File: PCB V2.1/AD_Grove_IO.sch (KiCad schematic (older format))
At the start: 0 parts

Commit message: SunLeaf Alpha 0.2 and KiCAD Port
SunLeaf rev 2 called Alhpa 0.2 or 0.2a is the main component of this
commit. The entire hardware project has been ported to KiCAD libaries
and all. 0.2a features a revised formfactor, better ESP module, and many
fixes over the original. This version will also be capable of OTA
updates.
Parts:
- added C32, C33, C34, C35: CL05B104JP5NNNC, PCB_Footprints:C0402, symbol CL05B104JP5NNNC
- added D10, D11, D12, D13: PESD3V3L2BT,215, PCB_Footprints:BAT20JFILM, symbol PESD3V3L2BT,215
- added J13, J14, J15, J16: S4B-PH-SM4-TB(LF)(SN), PCB_Footprints:S4B-PH-SM4-TB(LF)(SN), symbol S4B-PH-SM4-TB(LF)(SN)
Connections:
- net labels added: +3.3V, GND
- wire segments 0 -> 30

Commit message: Placement
Heavy progress on component placement in KiCAD for SunLEaf V2,
committing to save progress, nightly builds of KiCAD are very crash
prone.
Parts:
- D10, D11, D12, D13: footprint PCB_Footprints:BAT20JFILM -> PCB_Footprints:PESD3V3L2BT,215
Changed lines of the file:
@@
 F 0 "D10" V 4150 4675 60  0000 C CNN
 F 1 "PESD3V3L2BT,215" H 4375 4350 60  0000 C CNN
-F 2 "PCB_Footprints:BAT20JFILM" H 5650 6450 60  0001 C CNN
+F 2 "PCB_Footprints:PESD3V3L2BT,215" H 5650 6450 60  0001 C CNN
 F 3 "http://www.nxp.com/documents/data_sheet/PESDXL2BT_SER.pdf" H 5850 6575 60  0001 C CNN
 F 4 "0.15109 @ 6000" H 4075 4725 60  0001 C CNN "Cost"
@@
 F 0 "D11" V 4750 4675 60  0000 C CNN
 F 1 "PESD3V3L2BT,215" H 4975 4350 60  0000 C CNN
-F 2 "PCB_Footprints:BAT20JFILM" H 6250 6450 60  0001 C CNN
+F 2 "PCB_Footprints:PESD3V3L2BT,215" H 6250 6450 60  0001 C CNN
 F 3 "http://www.nxp.com/documents/data_sheet/PESDXL2BT_SER.pdf" H 6450 6575 60  0001 C CNN
 F 4 "0.15109 @ 6000" H 4675 4725 60  0001 C CNN "Cost"
@@
 F 0 "D12" V 5350 4675 60  0000 C CNN
 F 1 "PESD3V3L2BT,215" H 5575 4350 60  0000 C CNN
-F 2 "PCB_Footprints:BAT20JFILM" H 6850 6450 60  0001 C CNN
+F 2 "PCB_Footprints:PESD3V3L2BT,215" H 6850 6450 60  0001 C CNN
 F 3 "http://www.nxp.com/documents/data_sheet/PESDXL2BT_SER.pdf" H 7050 6575 60  0001 C CNN
 F 4 "0.15109 @ 6000" H 5275 4725 60  0001 C CNN "Cost"
@@
 F 0 "D13" V 5950 4675 60  0000 C CNN
 F 1 "PESD3V3L2BT,215" H 6175 4350 60  0000 C CNN
-F 2 "PCB_Footprints:BAT20JFILM" H 7450 6450 60  0001 C CNN
+F 2 "PCB_Footprints:PESD3V3L2BT,215" H 7450 6450 60  0001 C CNN
 F 3 "http://www.nxp.com/documents/data_sheet/PESDXL2BT_SER.pdf" H 7650 6575 60  0001 C CNN
 F 4 "0.15109 @ 6000" H 5875 4725 60  0001 C CNN "Cost"
@@
 Connection ~ 6100 2000
 $Comp
-L GND #PWR70
+L GND #PWR73
 U 1 1 57DACA24
 P 4225 4800
-F 0 "#PWR70" H 4225 4550 50  0001 C CNN
+F 0 "#PWR73" H 4225 4550 50  0001 C CNN
 F 1 "GND" H 4225 4650 50  0000 C CNN
 F 2 "" H 4225 4800 50  0000 C CNN
@@
 $EndComp
 $Comp
-L GND #PWR71
+L GND #PWR74
 U 1 1 57DACA56
 P 4825 4800
-F 0 "#PWR71" H 4825 4550 50  0001 C CNN
+F 0 "#PWR74" H 4825 4550 50  0001 C CNN
 F 1 "GND" H 4825 4650 50  0000 C CNN
 F 2 "" H 4825 4800 50  0000 C CNN
@@
 $EndComp
 $Comp
-L GND #PWR72
+L GND #PWR75
 U 1 1 57DACA7C
 P 5425 4800
-F 0 "#PWR72" H 5425 4550 50  0001 C CNN
+F 0 "#PWR75" H 5425 4550 50  0001 C CNN
 F 1 "GND" H 5425 4650 50  0000 C CNN
 F 2 "" H 5425 4800 50  0000 C CNN
@@
 $EndComp
 $Comp
-L GND #PWR73
+L GND #PWR76
 U 1 1 57DACAA2
 P 6025 4800
-F 0 "#PWR73" H 6025 4550 50  0001 C CNN
+F 0 "#PWR76" H 6025 4550 50  0001 C CNN
 F 1 "GND" H 6025 4650 50  0000 C CNN
 F 2 "" H 6025 4800 50  0000 C CNN
@@
 $EndComp
 $Comp
-L GND #PWR83
+L GND #PWR86
 U 1 1 57DACCA5
 P 10050 3675
-F 0 "#PWR83" H 10050 3425 50  0001 C CNN
+F 0 "#PWR86" H 10050 3425 50  0001 C CNN
 F 1 "GND" H 10050 3525 50  0000 C CNN
 F 2 "" H 10050 3675 50  0000 C CNN
@@
 $EndComp
 $Comp
-L GND #PWR82
+L GND #PWR85
 U 1 1 57DAD2A3
 P 10050 2975
-F 0 "#PWR82" H 10050 2725 50  0001 C CNN
+F 0 "#PWR85" H 10050 2725 50  0001 C CNN
 F 1 "GND" H 10050 2825 50  0000 C CNN
 F 2 "" H 10050 2975 50  0000 C CNN
@@
 $EndComp
 $Comp
-L GND #PWR81
+L GND #PWR84
 U 1 1 57DAD311
 P 10050 2250
-F 0 "#PWR81" H 10050 2000 50  0001 C CNN
+F 0 "#PWR84" H 10050 2000 50  0001 C CNN
 F 1 "GND" H 10050 2100 50  0000 C CNN
 F 2 "" H 10050 2250 50  0000 C CNN
@@
 $EndComp
 $Comp
-L GND #PWR80
+L GND #PWR83
 U 1 1 57DAD3C7
 P 10050 1525
-F 0 "#PWR80" H 10050 1275 50  0001 C CNN
+F 0 "#PWR83" H 10050 1275 50  0001 C CNN
 F 1 "GND" H 10050 1375 50  0000 C CNN
 F 2 "" H 10050 1525 50  0000 C CNN
@@
 	9950 1525 9950 1775
 $Comp
-L +3.3V #PWR76
+L +3.3V #PWR79
 U 1 1 57DAD7A9
 P 9700 4000
-F 0 "#PWR76" H 9700 3850 50  0001 C CNN
+F 0 "#PWR79" H 9700 3850 50  0001 C CNN
 F 1 "+3.3V" H 9700 4140 50  0000 C CNN
 F 2 "" H 9700 4000 50  0000 C CNN
@@
 	9700 4000 9950 4000
 $Comp
-L +3.3V #PWR79
+L +3.3V #PWR82
 U 1 1 57DAD8CB
 P 9725 3300
-F 0 "#PWR79" H 9725 3150 50  0001 C CNN
+F 0 "#PWR82" H 9725 3150 50  0001 C CNN
 F 1 "+3.3V" H 9725 3440 50  0000 C CNN
 F 2 "" H 9725 3300 50  0000 C CNN
@@
 	9950 3300 9725 3300
 $Comp
-L +3.3V #PWR78
+L +3.3V #PWR81
 U 1 1 57DAD9D1
 P 9725 2575
-F 0 "#PWR78" H 9725 2425 50  0001 C CNN
+F 0 "#PWR81" H 9725 2425 50  0001 C CNN
 F 1 "+3.3V" H 9725 2715 50  0000 C CNN
 F 2 "" H 9725 2575 50  0000 C CNN
@@
 	9725 2575 9950 2575
 $Comp
-L +3.3V #PWR77
+L +3.3V #PWR80
 U 1 1 57DADAE1
 P 9725 1850
-F 0 "#PWR77" H 9725 1700 50  0001 C CNN
+F 0 "#PWR80" H 9725 1700 50  0001 C CNN
 F 1 "+3.3V" H 9725 1990 50  0000 C CNN
 F 2 "" H 9725 1850 50  0000 C CNN
@@
 Connection ~ 9575 4475
 $Comp
-L +3.3V #PWR74
+L +3.3V #PWR77
 U 1 1 57DAE2C9
 P 9400 4475
-F 0 "#PWR74" H 9400 4325 50  0001 C CNN
+F 0 "#PWR77" H 9400 4325 50  0001 C CNN
 F 1 "+3.3V" H 9400 4615 50  0000 C CNN
 F 2 "" H 9400 4475 50  0000 C CNN
@@
 $EndComp
 $Comp
-L GND #PWR75
+L GND #PWR78
 U 1 1 57DAE2F8
 P 9400 4925
-F 0 "#PWR75" H 9400 4675 50  0001 C CNN
+F 0 "#PWR78" H 9400 4675 50  0001 C CNN
 F 1 "GND" H 9400 4775 50  0000 C CNN
 F 2 "" H 9400 4925 50  0000 C CNN

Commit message: Placement progress
Placement is 99% done board is being resized. Next commit TVS diode
pairs will be fliped and the baord further resized.
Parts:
- removed C32, C33, C34, C35: CL05B104JP5NNNC, PCB_Footprints:C0402, symbol CL05B104JP5NNNC
- removed J13, J14, J15, J16: S4B-PH-SM4-TB(LF)(SN), PCB_Footprints:S4B-PH-SM4-TB(LF)(SN), symbol S4B-PH-SM4-TB(LF)(SN)
- added J13, J14, J15, J16: B4B-PH-K-S(LF)(SN), PCB_Footprints:B4B-PH-K-S(LF)(SN), symbol B4B-PH-K-S(LF)(SN)
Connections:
- wire segments 30 -> 28

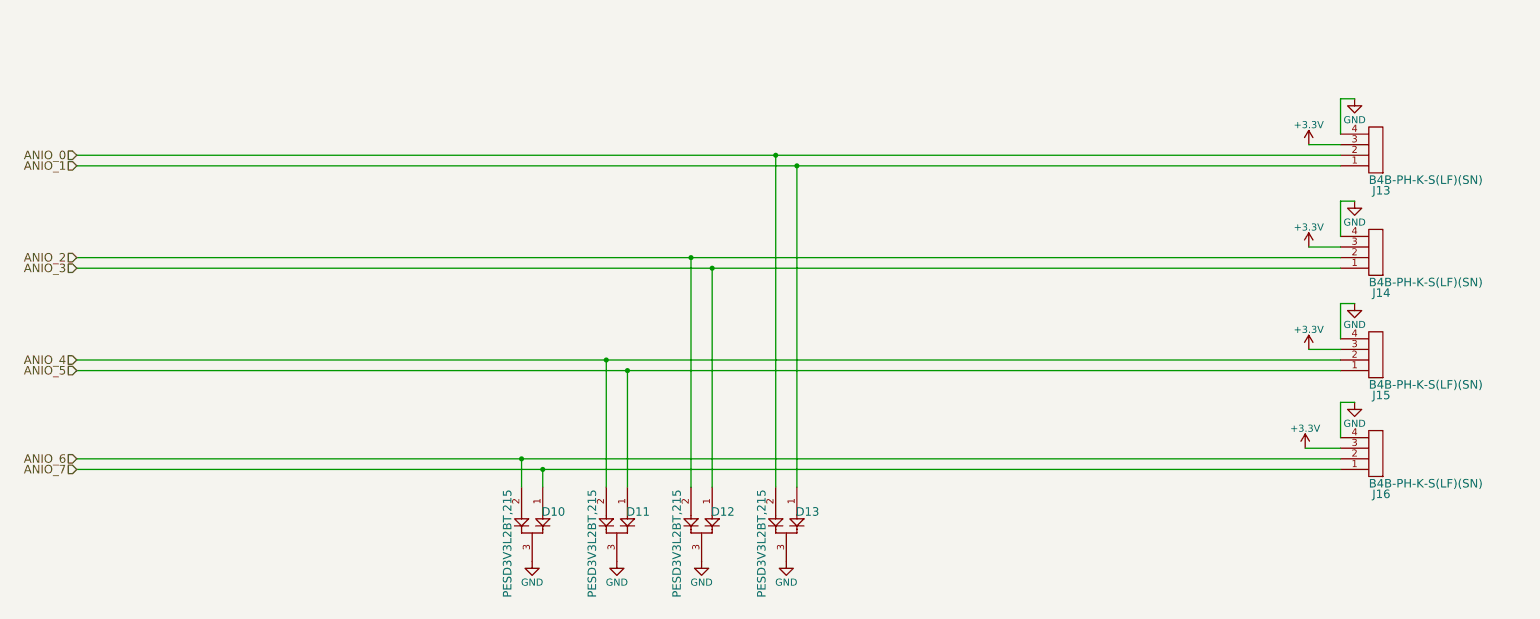
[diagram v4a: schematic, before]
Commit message: Internal Planes
Internal Planes added, small amount of routing left.
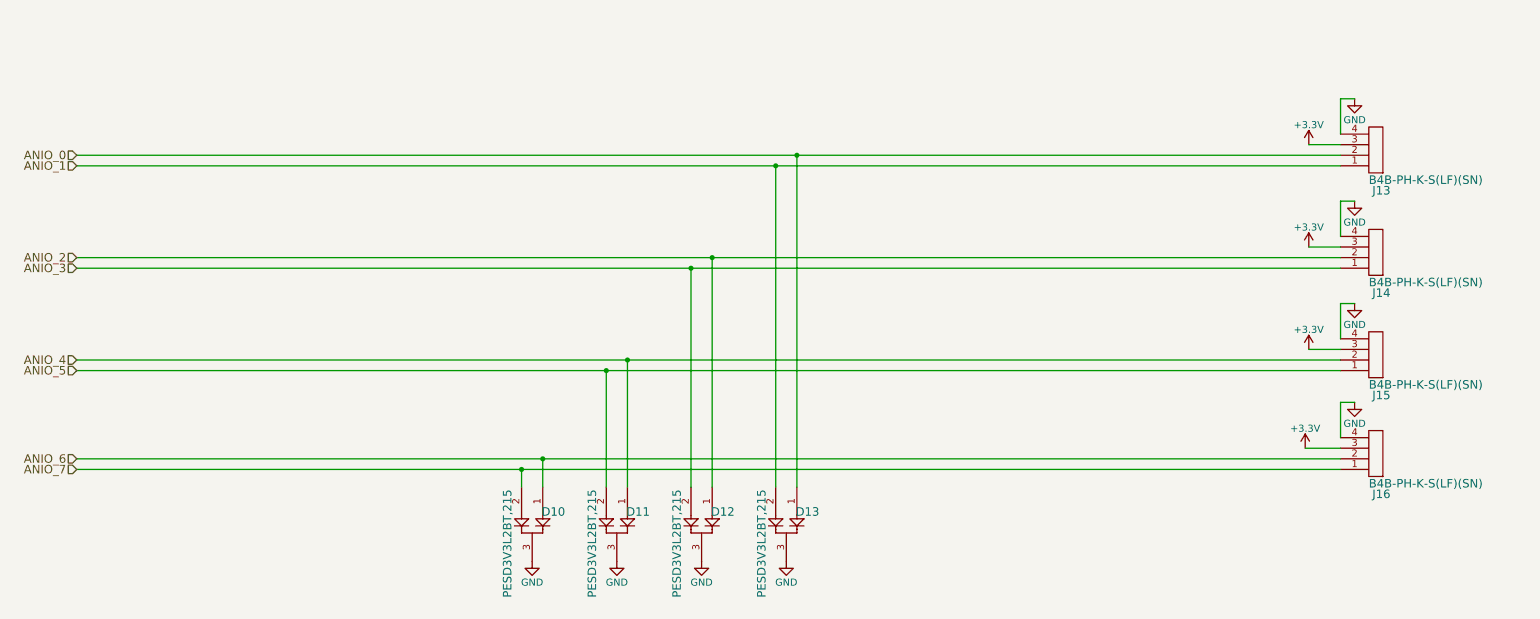
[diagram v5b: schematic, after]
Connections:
- net ANIO_0: now also D13.1; no longer D13.2
- net ANIO_1: now also D13.2; no longer D13.1
- net ANIO_2: now also D12.1; no longer D12.2
- net ANIO_3: now also D12.2; no longer D12.1
- net ANIO_4: now also D11.1; no longer D11.2
- net ANIO_5: now also D11.2; no longer D11.1
- net ANIO_6: now also D10.1; no longer D10.2
- net ANIO_7: now also D10.2; no longer D10.1
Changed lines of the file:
@@
 LIBS:contrib
 LIBS:valves
-LIBS:stm32
-LIBS:ESP8266
 LIBS:HydroPWNics_Lib
 LIBS:ESP32-footprints-Shem-Lib
@@
 $EndComp
 Wire Wire Line
-	9950 2650 1000 2650
-Wire Wire Line
-	9950 2725 1000 2725
-Wire Wire Line
-	9950 3375 1000 3375
-Wire Wire Line
-	9950 3450 1000 3450
-Wire Wire Line
-	9950 4075 1000 4075
-Wire Wire Line
-	1000 4150 9950 4150
-Wire Wire Line
-	9950 2000 1000 2000
-Wire Wire Line
-	9950 1925 1000 1925
-Wire Wire Line
-	4150 4275 4150 4075
-Connection ~ 4150 4075
-Wire Wire Line
-	4300 4275 4300 4150
-Connection ~ 4300 4150
-Wire Wire Line
-	4750 4275 4750 3375
-Connection ~ 4750 3375
-Wire Wire Line
-	4900 4275 4900 3450
-Connection ~ 4900 3450
-Wire Wire Line
-	5500 4275 5500 2725
-Connection ~ 5500 2725
-Wire Wire Line
-	5350 4275 5350 2650
-Connection ~ 5350 2650
-Wire Wire Line
-	5950 4275 5950 1925
-Connection ~ 5950 1925
-Wire Wire Line
-	6100 4275 6100 2000
-Connection ~ 6100 2000
+	9950 2650 5500 2650
+Wire Wire Line
+	5500 2650 1000 2650
+Wire Wire Line
+	9950 2725 5350 2725
+Wire Wire Line
+	5350 2725 1000 2725
+Wire Wire Line
+	9950 3375 4900 3375
+Wire Wire Line
+	4900 3375 1000 3375
+Wire Wire Line
+	9950 3450 4750 3450
+Wire Wire Line
+	4750 3450 1000 3450
+Wire Wire Line
+	9950 4075 4300 4075
+Wire Wire Line
+	4300 4075 1000 4075
+Wire Wire Line
+	1000 4150 4150 4150
+Wire Wire Line
+	4150 4150 9950 4150
+Wire Wire Line
+	9950 2000 5950 2000
+Wire Wire Line
+	5950 2000 1000 2000
+Wire Wire Line
+	9950 1925 6100 1925
+Wire Wire Line
+	6100 1925 1000 1925
+Connection ~ 4300 4075
+Connection ~ 4150 4150
+Connection ~ 4900 3375
+Connection ~ 4750 3450
+Connection ~ 5350 2725
+Connection ~ 5500 2650
+Connection ~ 6100 1925
 $Comp
 L GND #PWR73
@@
 	-1   0    0    1
 $EndComp
+Wire Wire Line
+	5950 4275 5950 2000
+Connection ~ 5950 2000
+Wire Wire Line
+	6100 1925 6100 4275
+Wire Wire Line
+	5500 2650 5500 4275
+Wire Wire Line
+	5350 4275 5350 2725
+Wire Wire Line
+	4900 3375 4900 4275
+Wire Wire Line
+	4900 4275 4900 4275
+Wire Wire Line
+	4750 3450 4750 4275
+Wire Wire Line
+	4300 4075 4300 4275
+Wire Wire Line
+	4150 4150 4150 4275
 $EndSCHEMATC

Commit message: OTA
This commit contains adjustments to the schematics for over the air
update/programming of STM32 via the ESP8266 using its internal
bootloader. The two processors have been wired together to suppor this
fucntions, they can toggle reset of eachother and load firmware over
UART. Still deciding what reset signal pin on the STM32 to use fo rthis
purpose, next commit.
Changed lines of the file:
@@
 LIBS:HydroPWNics_Lib
 LIBS:ESP32-footprints-Shem-Lib
+LIBS:ESP8266
 LIBS:SunLeaf_V2-cache
 EELAYER 25 0
@@
 $EndComp
 Wire Wire Line
-	9950 2650 5500 2650
-Wire Wire Line
-	5500 2650 1000 2650
-Wire Wire Line
-	9950 2725 5350 2725
-Wire Wire Line
-	5350 2725 1000 2725
-Wire Wire Line
-	9950 3375 4900 3375
-Wire Wire Line
-	4900 3375 1000 3375
-Wire Wire Line
-	9950 3450 4750 3450
-Wire Wire Line
-	4750 3450 1000 3450
-Wire Wire Line
-	9950 4075 4300 4075
-Wire Wire Line
-	4300 4075 1000 4075
-Wire Wire Line
-	1000 4150 4150 4150
-Wire Wire Line
-	4150 4150 9950 4150
-Wire Wire Line
-	9950 2000 5950 2000
-Wire Wire Line
-	5950 2000 1000 2000
-Wire Wire Line
-	9950 1925 6100 1925
-Wire Wire Line
-	6100 1925 1000 1925
+	1000 2650 9950 2650
+Wire Wire Line
+	1000 2725 9950 2725
+Wire Wire Line
+	1000 3375 9950 3375
+Wire Wire Line
+	1000 3450 9950 3450
+Wire Wire Line
+	1000 4075 9950 4075
+Wire Wire Line
+	1000 4150 9950 4150
+Wire Wire Line
+	1000 2000 9950 2000
+Wire Wire Line
+	1000 1925 9950 1925
 Connection ~ 4300 4075
 Connection ~ 4150 4150
@@
 Connection ~ 6100 1925
 $Comp
-L GND #PWR73
+L GND #PWR069
 U 1 1 57DACA24
 P 4225 4800
-F 0 "#PWR73" H 4225 4550 50  0001 C CNN
+F 0 "#PWR069" H 4225 4550 50  0001 C CNN
 F 1 "GND" H 4225 4650 50  0000 C CNN
 F 2 "" H 4225 4800 50  0000 C CNN
@@
 $EndComp
 $Comp
-L GND #PWR74
+L GND #PWR070
 U 1 1 57DACA56
 P 4825 4800
-F 0 "#PWR74" H 4825 4550 50  0001 C CNN
+F 0 "#PWR070" H 4825 4550 50  0001 C CNN
 F 1 "GND" H 4825 4650 50  0000 C CNN
 F 2 "" H 4825 4800 50  0000 C CNN
@@
 $EndComp
 $Comp
-L GND #PWR75
+L GND #PWR071
 U 1 1 57DACA7C
 P 5425 4800
-F 0 "#PWR75" H 5425 4550 50  0001 C CNN
+F 0 "#PWR071" H 5425 4550 50  0001 C CNN
 F 1 "GND" H 5425 4650 50  0000 C CNN
 F 2 "" H 5425 4800 50  0000 C CNN
@@
 $EndComp
 $Comp
-L GND #PWR76
+L GND #PWR072
 U 1 1 57DACAA2
 P 6025 4800
-F 0 "#PWR76" H 6025 4550 50  0001 C CNN
+F 0 "#PWR072" H 6025 4550 50  0001 C CNN
 F 1 "GND" H 6025 4650 50  0000 C CNN
 F 2 "" H 6025 4800 50  0000 C CNN
@@
 $EndComp
 $Comp
-L GND #PWR86
+L GND #PWR073
 U 1 1 57DACCA5
 P 10050 3675
-F 0 "#PWR86" H 10050 3425 50  0001 C CNN
+F 0 "#PWR073" H 10050 3425 50  0001 C CNN
 F 1 "GND" H 10050 3525 50  0000 C CNN
 F 2 "" H 10050 3675 50  0000 C CNN
@@
 $EndComp
 $Comp
-L GND #PWR85
+L GND #PWR074
 U 1 1 57DAD2A3
 P 10050 2975
-F 0 "#PWR85" H 10050 2725 50  0001 C CNN
+F 0 "#PWR074" H 10050 2725 50  0001 C CNN
 F 1 "GND" H 10050 2825 50  0000 C CNN
 F 2 "" H 10050 2975 50  0000 C CNN
@@
 $EndComp
 $Comp
-L GND #PWR84
+L GND #PWR075
 U 1 1 57DAD311
 P 10050 2250
-F 0 "#PWR84" H 10050 2000 50  0001 C CNN
+F 0 "#PWR075" H 10050 2000 50  0001 C CNN
 F 1 "GND" H 10050 2100 50  0000 C CNN
 F 2 "" H 10050 2250 50  0000 C CNN
@@
 $EndComp
 $Comp
-L GND #PWR83
+L GND #PWR076
 U 1 1 57DAD3C7
 P 10050 1525
-F 0 "#PWR83" H 10050 1275 50  0001 C CNN
+F 0 "#PWR076" H 10050 1275 50  0001 C CNN
 F 1 "GND" H 10050 1375 50  0000 C CNN
 F 2 "" H 10050 1525 50  0000 C CNN
@@
 	9950 1525 9950 1775
 $Comp
-L +3.3V #PWR79
+L +3.3V #PWR077
 U 1 1 57DAD7A9
 P 9700 4000
-F 0 "#PWR79" H 9700 3850 50  0001 C CNN
+F 0 "#PWR077" H 9700 3850 50  0001 C CNN
 F 1 "+3.3V" H 9700 4140 50  0000 C CNN
 F 2 "" H 9700 4000 50  0000 C CNN
@@
 	9700 4000 9950 4000
 $Comp
-L +3.3V #PWR82
+L +3.3V #PWR078
 U 1 1 57DAD8CB
 P 9725 3300
-F 0 "#PWR82" H 9725 3150 50  0001 C CNN
+F 0 "#PWR078" H 9725 3150 50  0001 C CNN
 F 1 "+3.3V" H 9725 3440 50  0000 C CNN
 F 2 "" H 9725 3300 50  0000 C CNN
@@
 	9950 3300 9725 3300
 $Comp
-L +3.3V #PWR81
+L +3.3V #PWR079
 U 1 1 57DAD9D1
 P 9725 2575
-F 0 "#PWR81" H 9725 2425 50  0001 C CNN
+F 0 "#PWR079" H 9725 2425 50  0001 C CNN
 F 1 "+3.3V" H 9725 2715 50  0000 C CNN
 F 2 "" H 9725 2575 50  0000 C CNN
@@
 	9725 2575 9950 2575
 $Comp
-L +3.3V #PWR80
+L +3.3V #PWR080
 U 1 1 57DADAE1
 P 9725 1850
-F 0 "#PWR80" H 9725 1700 50  0001 C CNN
+F 0 "#PWR080" H 9725 1700 50  0001 C CNN
 F 1 "+3.3V" H 9725 1990 50  0000 C CNN
 F 2 "" H 9725 1850 50  0000 C CNN
@@
 	4900 3375 4900 4275
 Wire Wire Line
-	4900 4275 4900 4275
-Wire Wire Line
 	4750 3450 4750 4275

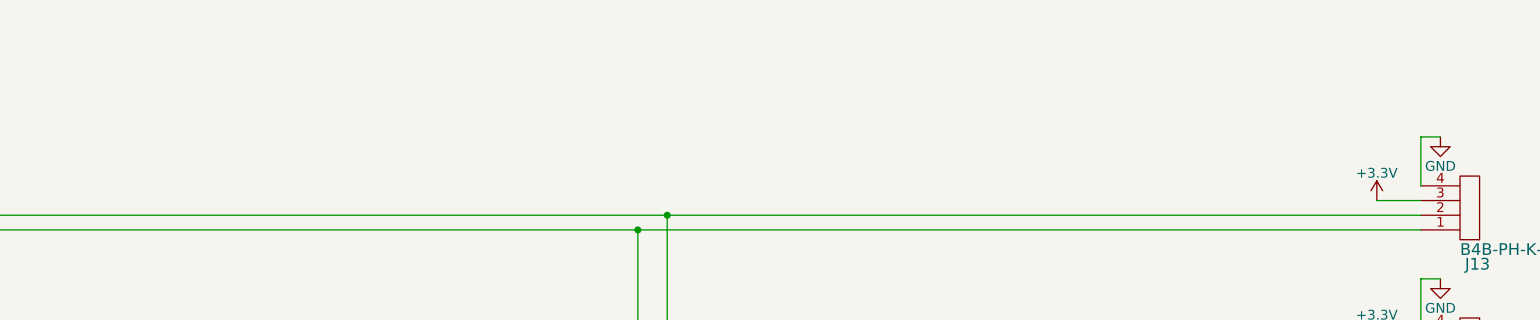
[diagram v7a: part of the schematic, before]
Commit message: App Notes
App notes added to datasheets folder.
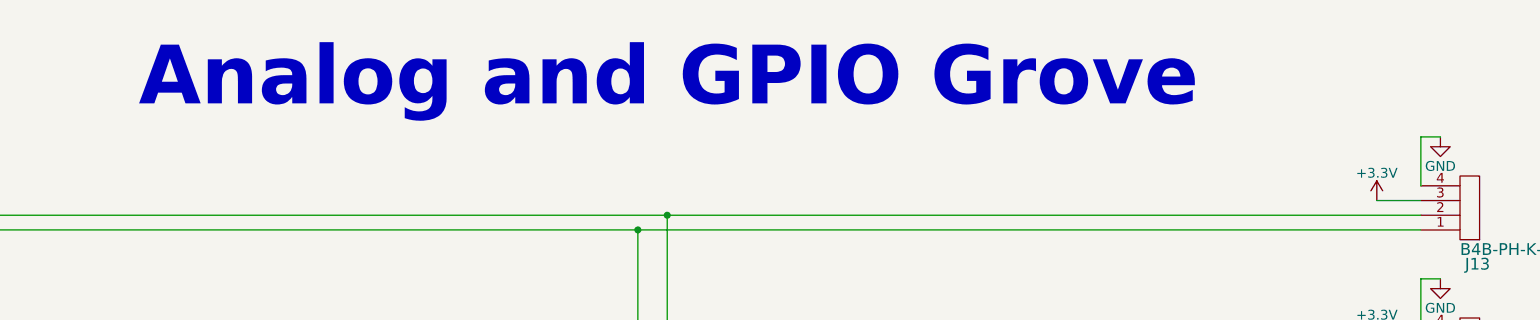
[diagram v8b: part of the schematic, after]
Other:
- note added: "Analog and GPIO Grove"
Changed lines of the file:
@@
 Connection ~ 6100 1925
 $Comp
-L GND #PWR71
+L GND #PWR072
 U 1 1 57DACA24
 P 4225 4800
-F 0 "#PWR71" H 4225 4550 50  0001 C CNN
+F 0 "#PWR072" H 4225 4550 50  0001 C CNN
 F 1 "GND" H 4225 4650 50  0000 C CNN
 F 2 "" H 4225 4800 50  0000 C CNN
@@
 $EndComp
 $Comp
-L GND #PWR72
+L GND #PWR073
 U 1 1 57DACA56
 P 4825 4800
-F 0 "#PWR72" H 4825 4550 50  0001 C CNN
+F 0 "#PWR073" H 4825 4550 50  0001 C CNN
 F 1 "GND" H 4825 4650 50  0000 C CNN
 F 2 "" H 4825 4800 50  0000 C CNN
@@
 $EndComp
 $Comp
-L GND #PWR73
+L GND #PWR074
 U 1 1 57DACA7C
 P 5425 4800
-F 0 "#PWR73" H 5425 4550 50  0001 C CNN
+F 0 "#PWR074" H 5425 4550 50  0001 C CNN
 F 1 "GND" H 5425 4650 50  0000 C CNN
 F 2 "" H 5425 4800 50  0000 C CNN
@@
 $EndComp
 $Comp
-L GND #PWR74
+L GND #PWR075
 U 1 1 57DACAA2
 P 6025 4800
-F 0 "#PWR74" H 6025 4550 50  0001 C CNN
+F 0 "#PWR075" H 6025 4550 50  0001 C CNN
 F 1 "GND" H 6025 4650 50  0000 C CNN
 F 2 "" H 6025 4800 50  0000 C CNN
@@
 $EndComp
 $Comp
-L GND #PWR82
+L GND #PWR076
 U 1 1 57DACCA5
 P 10050 3675
-F 0 "#PWR82" H 10050 3425 50  0001 C CNN
+F 0 "#PWR076" H 10050 3425 50  0001 C CNN
 F 1 "GND" H 10050 3525 50  0000 C CNN
 F 2 "" H 10050 3675 50  0000 C CNN
@@
 $EndComp
 $Comp
-L GND #PWR81
+L GND #PWR077
 U 1 1 57DAD2A3
 P 10050 2975
-F 0 "#PWR81" H 10050 2725 50  0001 C CNN
+F 0 "#PWR077" H 10050 2725 50  0001 C CNN
 F 1 "GND" H 10050 2825 50  0000 C CNN
 F 2 "" H 10050 2975 50  0000 C CNN
@@
 $EndComp
 $Comp
-L GND #PWR80
+L GND #PWR078
 U 1 1 57DAD311
 P 10050 2250
-F 0 "#PWR80" H 10050 2000 50  0001 C CNN
+F 0 "#PWR078" H 10050 2000 50  0001 C CNN
 F 1 "GND" H 10050 2100 50  0000 C CNN
 F 2 "" H 10050 2250 50  0000 C CNN
@@
 $EndComp
 $Comp
-L GND #PWR79
+L GND #PWR079
 U 1 1 57DAD3C7
 P 10050 1525
-F 0 "#PWR79" H 10050 1275 50  0001 C CNN
+F 0 "#PWR079" H 10050 1275 50  0001 C CNN
 F 1 "GND" H 10050 1375 50  0000 C CNN
 F 2 "" H 10050 1525 50  0000 C CNN
@@
 	9950 1525 9950 1775
 $Comp
-L +3.3V #PWR75
+L +3.3V #PWR080
 U 1 1 57DAD7A9
 P 9700 4000
-F 0 "#PWR75" H 9700 3850 50  0001 C CNN
+F 0 "#PWR080" H 9700 3850 50  0001 C CNN
 F 1 "+3.3V" H 9700 4140 50  0000 C CNN
 F 2 "" H 9700 4000 50  0000 C CNN
@@
 	9700 4000 9950 4000
 $Comp
-L +3.3V #PWR78
+L +3.3V #PWR081
 U 1 1 57DAD8CB
 P 9725 3300
-F 0 "#PWR78" H 9725 3150 50  0001 C CNN
+F 0 "#PWR081" H 9725 3150 50  0001 C CNN
 F 1 "+3.3V" H 9725 3440 50  0000 C CNN
 F 2 "" H 9725 3300 50  0000 C CNN
@@
 	9950 3300 9725 3300
 $Comp
-L +3.3V #PWR77
+L +3.3V #PWR082
 U 1 1 57DAD9D1
 P 9725 2575
-F 0 "#PWR77" H 9725 2425 50  0001 C CNN
+F 0 "#PWR082" H 9725 2425 50  0001 C CNN
 F 1 "+3.3V" H 9725 2715 50  0000 C CNN
 F 2 "" H 9725 2575 50  0000 C CNN
@@
 	9725 2575 9950 2575
 $Comp
-L +3.3V #PWR76
+L +3.3V #PWR083
 U 1 1 57DADAE1
 P 9725 1850
-F 0 "#PWR76" H 9725 1700 50  0001 C CNN
+F 0 "#PWR083" H 9725 1700 50  0001 C CNN
 F 1 "+3.3V" H 9725 1990 50  0000 C CNN
 F 2 "" H 9725 1850 50  0000 C CNN
@@
 Wire Wire Line
 	4150 4150 4150 4275
+Text Notes 3400 1400 0    300  ~ 60
+Analog and GPIO Grove
 $EndSCHEMATC
